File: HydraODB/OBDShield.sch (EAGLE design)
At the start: 29 parts, among them CN1 8p-2.54, J1 HYDRABUS_SHIELD_CON_HEADER_2X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, J2 HYDRABUS_SHIELD_CON_HEADER_2X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, J3 HYDRABUS_SHIELD_CON_HEADER_2X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, K1 TS-1188E, U1 SN65HVD233DG4, U2 SN65HVD233DG4, U3 CJ78M05-to252

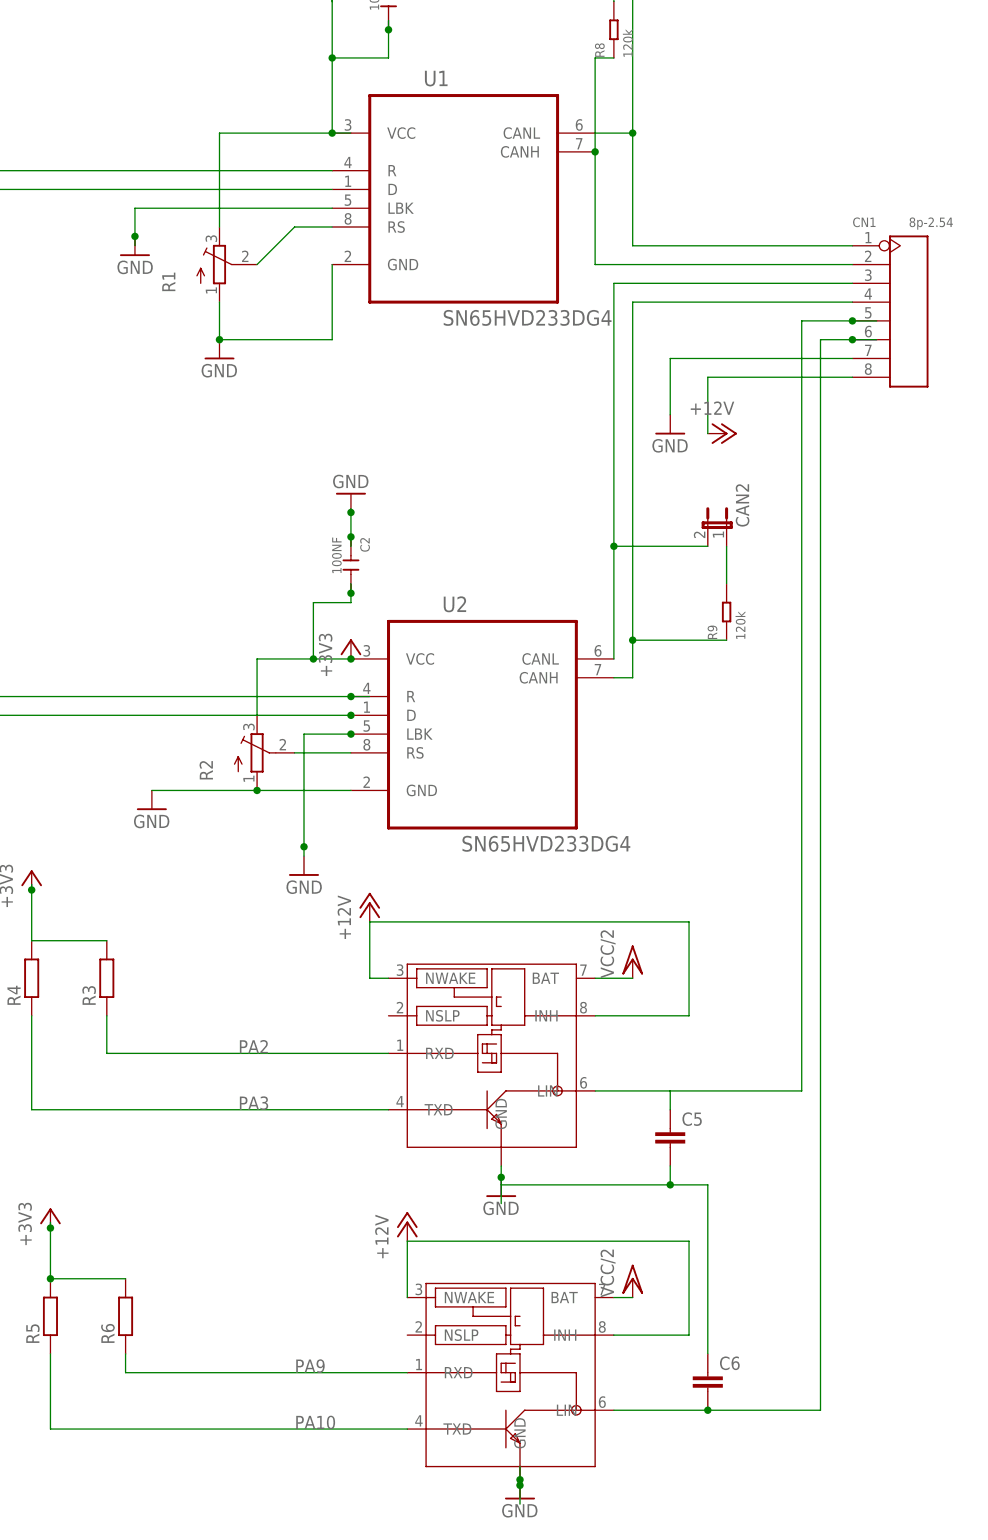
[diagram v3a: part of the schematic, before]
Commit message: Corrections for CAN and LIN buses
Deleted connections between trimmers and VCC
Added decap on LIN tranceivers
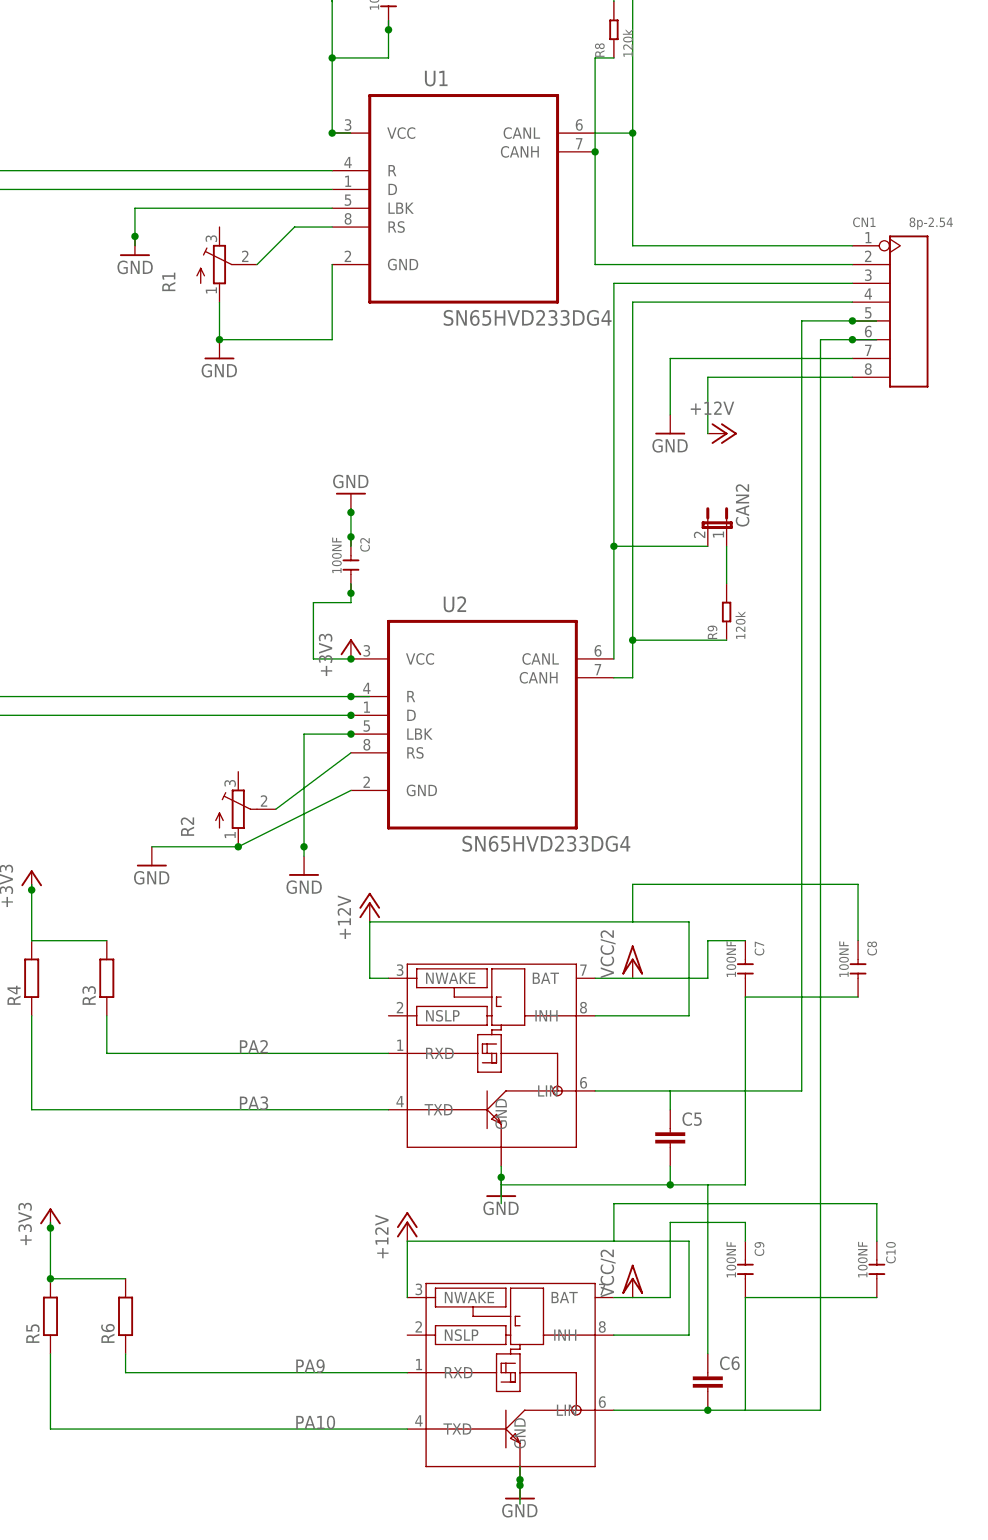
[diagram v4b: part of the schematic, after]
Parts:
- added C10, C7, C8, C9: 100NF, Seeed-OPL-Capacitor:CERAMIC-100NF-50V-20%-Y5V(0805)
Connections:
- net +12V: now also C10.1, C8.1
- net +3V3: no longer R1.E, R2.E
- net GND: now also C7.2, C8.2
- net N$7: now also C10.2, C9.2
- net VCC/2: now also C7.1, C9.1
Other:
- moved on the sheet: R2
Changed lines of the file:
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@@
 <?xml version="1.0" encoding="utf-8"?>
 <!DOCTYPE eagle SYSTEM "eagle.dtd">
-<eagle version="8.1.0">
+<eagle version="8.3.1">
 <drawing>
 <settings>
 <setting alwaysvectorfont="no"/>
+<setting keepoldvectorfont="yes"/>
 <setting verticaltext="up"/>
 </settings>
@@
 </variantdefs>
 <classes>
-<class number="0" name="default" width="0.254" drill="0.3302">
+<class number="0" name="default" width="0.254" drill="0.5">
 <clearance class="0" value="0.2032"/>
 </class>
-<class number="1" name="POWER" width="0.254" drill="0.3302">
+<class number="1" name="POWER" width="0.254" drill="0.5">
 <clearance class="1" value="0.2032"/>
 </class>
-<class number="2" name="VDD" width="0.3302" drill="0.3302">
+<class number="2" name="VDD" width="0.3302" drill="0.5">
 <clearance class="2" value="0.2032"/>
+</class>
+<class number="3" name="CAN" width="0.3302" drill="0.5">
+<clearance class="3" value="0.3048"/>
 </class>
 </classes>
@@
 <part name="+3V4" library="supply1" deviceset="+3V3" device=""/>
 <part name="+3V7" library="supply1" deviceset="+3V3" device=""/>
+<part name="C7" library="Seeed-OPL-Capacitor" deviceset="CERAMIC-100NF-50V-20%-Y5V(0805)" device="" value="100NF"/>
+<part name="C8" library="Seeed-OPL-Capacitor" deviceset="CERAMIC-100NF-50V-20%-Y5V(0805)" device="" value="100NF"/>
+<part name="C9" library="Seeed-OPL-Capacitor" deviceset="CERAMIC-100NF-50V-20%-Y5V(0805)" device="" value="100NF"/>
+<part name="C10" library="Seeed-OPL-Capacitor" deviceset="CERAMIC-100NF-50V-20%-Y5V(0805)" device="" value="100NF"/>
 </parts>
 <sheets>
@@
 <instance part="U2" gate="A" x="177.8" y="38.1"/>
 <instance part="R1" gate="1" x="142.24" y="96.52"/>
-<instance part="R2" gate="1" x="147.32" y="30.48"/>
+<instance part="R2" gate="1" x="144.78" y="22.86"/>
 <instance part="+3V1" gate="G$1" x="160.02" y="45.72"/>
 <instance part="GND2" gate="1" x="142.24" y="83.82"/>
@@
 <instance part="P+2" gate="1" x="210.82" y="73.66" rot="R270"/>
 <instance part="GND8" gate="1" x="203.2" y="73.66"/>
-<instance part="GND10" gate="1" x="133.096" y="22.86"/>
+<instance part="GND10" gate="1" x="133.096" y="15.24"/>
 <instance part="GND11" gate="1" x="130.81" y="97.79" rot="MR0"/>
 <instance part="GND12" gate="1" x="153.67" y="13.97" rot="MR0"/>
@@
 <instance part="+3V4" gate="G$1" x="116.84" y="14.478"/>
 <instance part="+3V7" gate="G$1" x="119.38" y="-31.242"/>
+<instance part="C7" gate="G$1" x="213.36" y="1.27" rot="R270"/>
+<instance part="C8" gate="G$1" x="228.6" y="1.27" rot="R270"/>
+<instance part="C9" gate="G$1" x="213.36" y="-39.37" rot="R270"/>
+<instance part="C10" gate="G$1" x="231.14" y="-39.37" rot="R270"/>
 </instances>
 <busses>
@@
 <wire x1="157.48" y1="138.43" x2="157.48" y2="132.08" width="0.1524" layer="91"/>
 <junction x="157.48" y="138.43"/>
-<pinref part="R1" gate="1" pin="E"/>
-<wire x1="142.24" y1="101.6" x2="142.24" y2="114.3" width="0.1524" layer="91"/>
-<wire x1="142.24" y1="114.3" x2="157.48" y2="114.3" width="0.1524" layer="91"/>
 <junction x="157.48" y="114.3"/>
 <wire x1="157.48" y1="114.3" x2="160.02" y2="114.3" width="0.1524" layer="91"/>
@@
 <segment>
 <pinref part="U2" gate="A" pin="VCC"/>
-<pinref part="R2" gate="1" pin="E"/>
 <wire x1="160.02" y1="43.18" x2="154.94" y2="43.18" width="0.1524" layer="91"/>
-<wire x1="154.94" y1="43.18" x2="147.32" y2="43.18" width="0.1524" layer="91"/>
-<wire x1="147.32" y1="43.18" x2="147.32" y2="35.56" width="0.1524" layer="91"/>
 <pinref part="+3V1" gate="G$1" pin="+3V3"/>
 <junction x="160.02" y="43.18"/>
-<junction x="154.94" y="43.18"/>
 <wire x1="154.94" y1="43.18" x2="154.94" y2="50.8" width="0.1524" layer="91"/>
 <wire x1="154.94" y1="50.8" x2="160.02" y2="50.8" width="0.1524" layer="91"/>
@@
 <segment>
 <pinref part="U2" gate="A" pin="GND"/>
-<wire x1="160.02" y1="25.4" x2="147.32" y2="25.4" width="0.1524" layer="91"/>
+<wire x1="160.02" y1="25.4" x2="144.78" y2="17.78" width="0.1524" layer="91"/>
 <pinref part="R2" gate="1" pin="A"/>
 <pinref part="GND10" gate="1" pin="GND"/>
-<wire x1="133.096" y1="25.4" x2="147.32" y2="25.4" width="0.1524" layer="91"/>
-<junction x="147.32" y="25.4"/>
+<wire x1="133.096" y1="17.78" x2="144.78" y2="17.78" width="0.1524" layer="91"/>
+<junction x="144.78" y="17.78"/>
 </segment>
 <segment>
@@
 <wire x1="208.28" y1="-27.94" x2="208.28" y2="-50.8" width="0.1524" layer="91"/>
 <junction x="203.2" y="-27.94"/>
+<pinref part="C7" gate="G$1" pin="2"/>
+<wire x1="208.28" y1="-27.94" x2="213.36" y2="-27.94" width="0.1524" layer="91"/>
+<wire x1="213.36" y1="-27.94" x2="213.36" y2="-2.54" width="0.1524" layer="91"/>
+<pinref part="C8" gate="G$1" pin="2"/>
+<wire x1="213.36" y1="-2.54" x2="228.6" y2="-2.54" width="0.1524" layer="91"/>
 </segment>
 <segment>
@@
 </segment>
 </net>
-<net name="N$10" class="0">
+<net name="N$10" class="3">
 <segment>
 <pinref part="U1" gate="A" pin="CANH"/>
@@
 </segment>
 </net>
-<net name="N$11" class="0">
+<net name="N$11" class="3">
 <segment>
 <pinref part="U2" gate="A" pin="CANL"/>
@@
 <wire x1="165.1" y1="0" x2="162.56" y2="0" width="0.1524" layer="91"/>
 <wire x1="162.56" y1="0" x2="162.56" y2="7.62" width="0.1524" layer="91"/>
-<wire x1="162.56" y1="7.62" x2="205.74" y2="7.62" width="0.1524" layer="91"/>
+<wire x1="162.56" y1="7.62" x2="198.12" y2="7.62" width="0.1524" layer="91"/>
+<wire x1="198.12" y1="7.62" x2="205.74" y2="7.62" width="0.1524" layer="91"/>
 <wire x1="205.74" y1="7.62" x2="205.74" y2="-5.08" width="0.1524" layer="91"/>
 <pinref part="U$1" gate="G$1" pin="INH"/>
 <wire x1="205.74" y1="-5.08" x2="193.04" y2="-5.08" width="0.1524" layer="91"/>
+<wire x1="198.12" y1="7.62" x2="198.12" y2="12.7" width="0.1524" layer="91"/>
+<pinref part="C8" gate="G$1" pin="1"/>
+<wire x1="198.12" y1="12.7" x2="228.6" y2="12.7" width="0.1524" layer="91"/>
+<wire x1="228.6" y1="12.7" x2="228.6" y2="5.08" width="0.1524" layer="91"/>
 </segment>
 <segment>
@@
 <pinref part="P+9" gate="1" pin="+12V"/>
 <wire x1="167.64" y1="-43.18" x2="167.64" y2="-35.56" width="0.1524" layer="91"/>
-<wire x1="167.64" y1="-35.56" x2="205.74" y2="-35.56" width="0.1524" layer="91"/>
+<wire x1="195.58" y1="-35.56" x2="205.74" y2="-35.56" width="0.1524" layer="91"/>
 <wire x1="205.74" y1="-35.56" x2="205.74" y2="-48.26" width="0.1524" layer="91"/>
 <pinref part="U$2" gate="G$1" pin="INH"/>
 <wire x1="205.74" y1="-48.26" x2="195.58" y2="-48.26" width="0.1524" layer="91"/>
+<wire x1="167.64" y1="-35.56" x2="195.58" y2="-35.56" width="0.1524" layer="91"/>
+<wire x1="195.58" y1="-35.56" x2="195.58" y2="-30.48" width="0.1524" layer="91"/>
+<pinref part="C10" gate="G$1" pin="1"/>
+<wire x1="195.58" y1="-30.48" x2="231.14" y2="-30.48" width="0.1524" layer="91"/>
+<wire x1="231.14" y1="-30.48" x2="231.14" y2="-35.56" width="0.1524" layer="91"/>
 </segment>
 </net>
@@
 <pinref part="R2" gate="1" pin="S"/>
 <pinref part="U2" gate="A" pin="RS"/>
-<wire x1="152.4" y1="30.48" x2="160.02" y2="30.48" width="0.1524" layer="91"/>
+<wire x1="149.86" y1="22.86" x2="160.02" y2="30.48" width="0.1524" layer="91"/>
 </segment>
 </net>
@@
 </segment>
 </net>
-<net name="N$9" class="0">
+<net name="N$9" class="3">
 <segment>
 <wire x1="198.12" y1="99.06" x2="198.12" y2="114.3" width="0.1524" layer="91"/>
@@
 </segment>
 </net>
-<net name="N$12" class="0">
+<net name="N$12" class="3">
 <segment>
 <pinref part="U2" gate="A" pin="CANH"/>
@@
 <pinref part="P+5" gate="G$1" pin="VCC/2"/>
 <wire x1="193.04" y1="0" x2="198.12" y2="0" width="0.1524" layer="91"/>
+<wire x1="198.12" y1="0" x2="208.28" y2="0" width="0.1524" layer="91"/>
+<wire x1="208.28" y1="0" x2="208.28" y2="5.08" width="0.1524" layer="91"/>
+<pinref part="C7" gate="G$1" pin="1"/>
+<wire x1="208.28" y1="5.08" x2="213.36" y2="5.08" width="0.1524" layer="91"/>
 </segment>
 <segment>
@@
 <pinref part="P+6" gate="G$1" pin="VCC/2"/>
 <wire x1="198.12" y1="-43.18" x2="195.58" y2="-43.18" width="0.1524" layer="91"/>
+<wire x1="198.12" y1="-43.18" x2="203.2" y2="-43.18" width="0.1524" layer="91"/>
+<wire x1="203.2" y1="-43.18" x2="203.2" y2="-33.02" width="0.1524" layer="91"/>
+<pinref part="C9" gate="G$1" pin="1"/>
+<wire x1="203.2" y1="-33.02" x2="213.36" y2="-33.02" width="0.1524" layer="91"/>
+<wire x1="213.36" y1="-33.02" x2="213.36" y2="-35.56" width="0.1524" layer="91"/>
 </segment>
 </net>
@@
 <pinref part="U$2" gate="G$1" pin="LIN"/>
 <wire x1="195.58" y1="-58.42" x2="208.28" y2="-58.42" width="0.1524" layer="91"/>
-<wire x1="208.28" y1="-58.42" x2="223.52" y2="-58.42" width="0.1524" layer="91"/>
+<wire x1="208.28" y1="-58.42" x2="213.36" y2="-58.42" width="0.1524" layer="91"/>
+<wire x1="213.36" y1="-58.42" x2="223.52" y2="-58.42" width="0.1524" layer="91"/>
 <wire x1="223.52" y1="-58.42" x2="223.52" y2="86.36" width="0.1524" layer="91"/>
 <wire x1="223.52" y1="86.36" x2="227.838" y2="86.36" width="0.1524" layer="91"/>
@@
 <wire x1="227.838" y1="86.36" x2="231.14" y2="86.36" width="0.1524" layer="91"/>
 <junction x="227.838" y="86.36"/>
-</segment>
-</net>
+<pinref part="C9" gate="G$1" pin="2"/>
+<wire x1="213.36" y1="-58.42" x2="213.36" y2="-43.18" width="0.1524" layer="91"/>
+<pinref part="C10" gate="G$1" pin="2"/>
+<wire x1="213.36" y1="-43.18" x2="231.14" y2="-43.18" width="0.1524" layer="91"/>
+</segment>
+</net>
